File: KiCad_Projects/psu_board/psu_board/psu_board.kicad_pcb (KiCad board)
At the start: 2 copper layers, 21 parts, among them J1 Conn_01x02_Female, J2 Conn_01x02_Female, J3 Conn_01x02_Female, SW1 SW_DIP_x01, SW2 SW_DIP_x01, U1 OKL-T_6-W12N-C

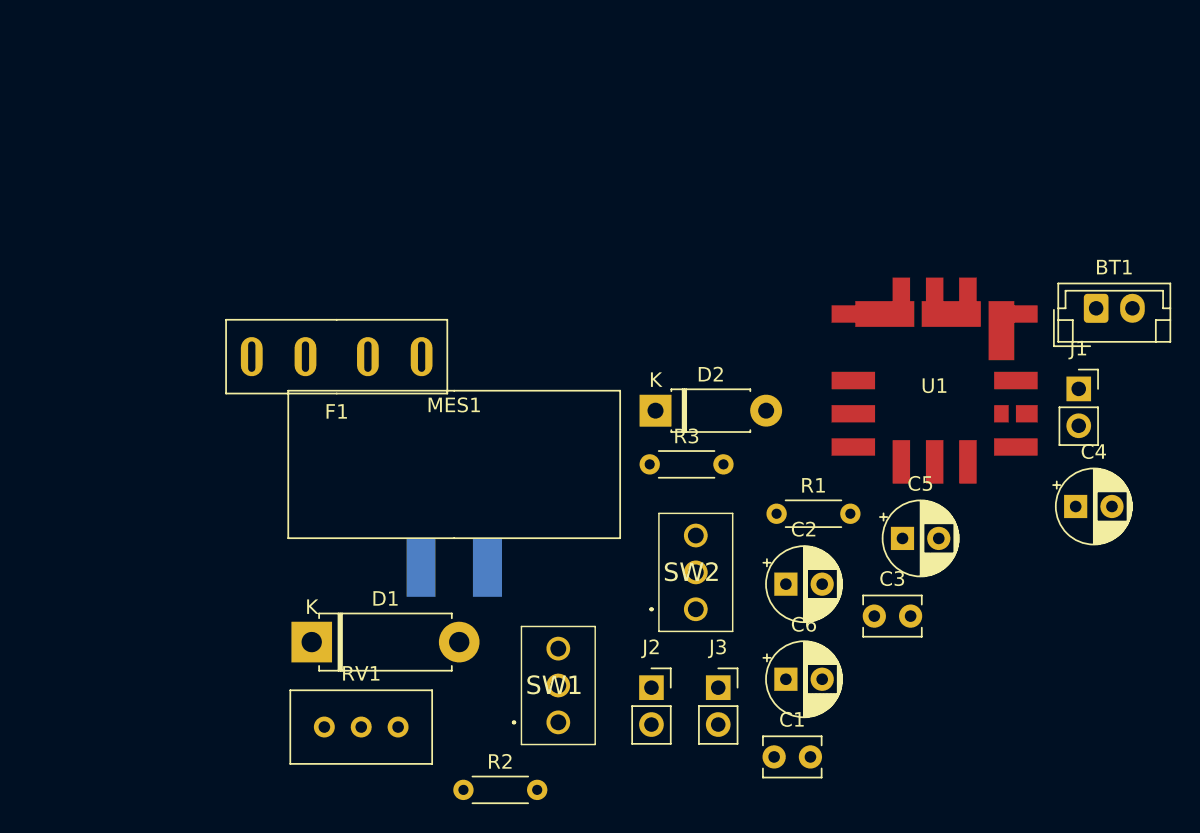
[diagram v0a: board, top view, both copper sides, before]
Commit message: 基盤データの更新
フットプリントの更新、電源基盤の部品の配置
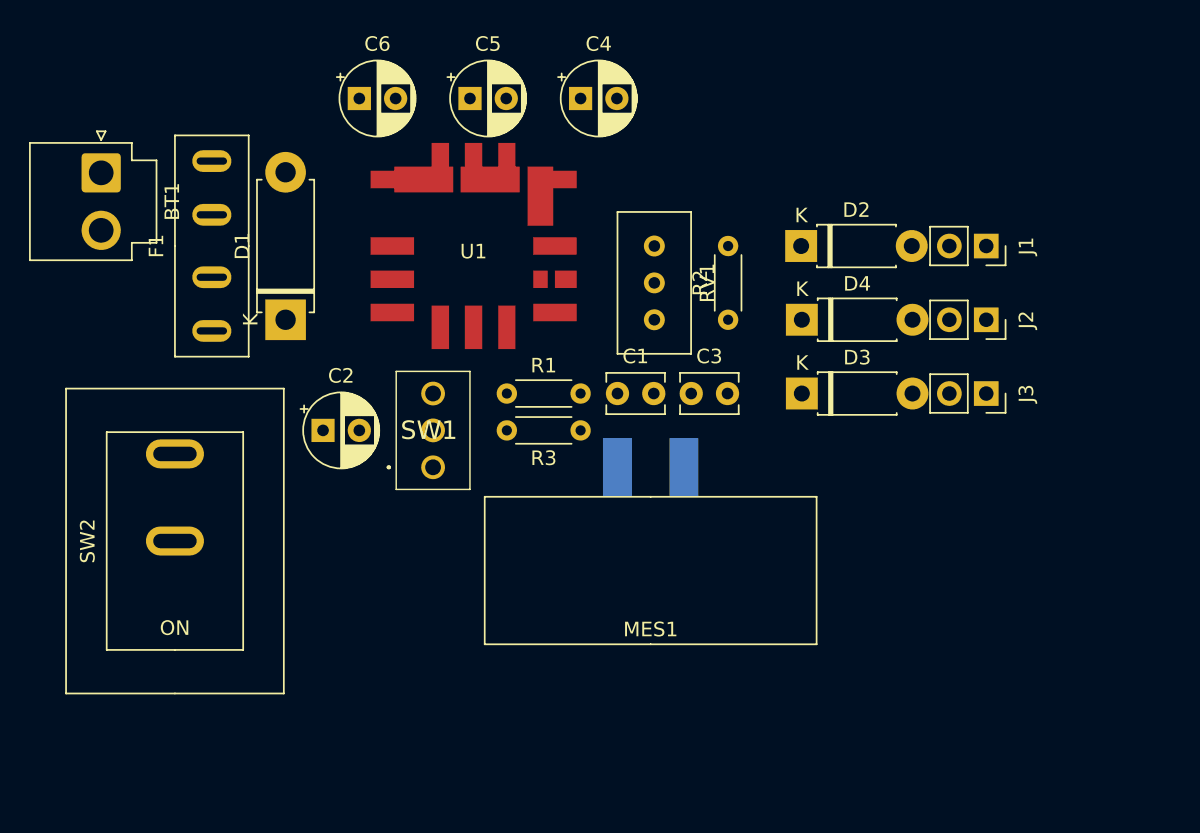
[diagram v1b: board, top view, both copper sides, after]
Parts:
- added D3: D, Diode_THT:D_DO-41_SOD81_P7.62mm_Horizontal, F.Cu at (154.9, 83.8)
- added D4: D, Diode_THT:D_DO-41_SOD81_P7.62mm_Horizontal, F.Cu at (154.9, 78.7)
- BT1: footprint Connector_JST:JST_EH_B2B-EH-A_1x02_P2.50mm_Vertical -> Connector_JST:JST_VH_B2P-VH-B_1x02_P3.96mm_Vertical
- SW2: footprint Lib:2MS1T2B4M2QES -> Lib:DS-850k
- moved BT1 69.2 mm to (106.7, 68.6), turned to -90 degrees
- moved C6 49.6 mm to (124.5, 63.5)
- moved C4 44.2 mm to (139.7, 63.5)
- moved C5 42.5 mm to (132.1, 63.5)
- moved R2 37.2 mm to (149.9, 78.7), turned to 90 degrees
- moved SW2 36.2 mm to (111.8, 94.0), turned to -90 degrees
- moved J2 34.3 mm to (167.6, 78.7), turned to -90 degrees
- moved C2 33.6 mm to (122.0, 86.4)
- moved RV1 33.1 mm to (144.8, 78.7), turned to -90 degrees
- moved U1 33.1 mm to (126.2, 79.8)
- moved J3 27.4 mm to (167.6, 83.8), turned to -90 degrees
- moved C1 27.3 mm to (142.2, 83.8)
- moved D1 22.3 mm to (119.4, 78.7), turned to 90 degrees
- moved MES1 22.1 mm to (144.5, 101.1), turned to 180 degrees
- moved R1 20.3 mm to (134.6, 83.8)
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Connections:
- C3 pad 1: Net-(C3-Pad1) -> +5V
- D2 pad 1: +5V -> Net-(D2-Pad1)
- D2 pad 2: Net-(C3-Pad1) -> +7.5V
- J1 pad 1: +7.5V -> Net-(D2-Pad1)
- J2 pad 1: +7.5V -> Net-(D4-Pad1)
- J3 pad 1: +5V -> Net-(D3-Pad1)
- R3 pad 1: Net-(C3-Pad1) -> +5V
- U1 pad 4: Net-(C3-Pad1) -> +5V
- U1 pad 5: Net-(C3-Pad1) -> +5V

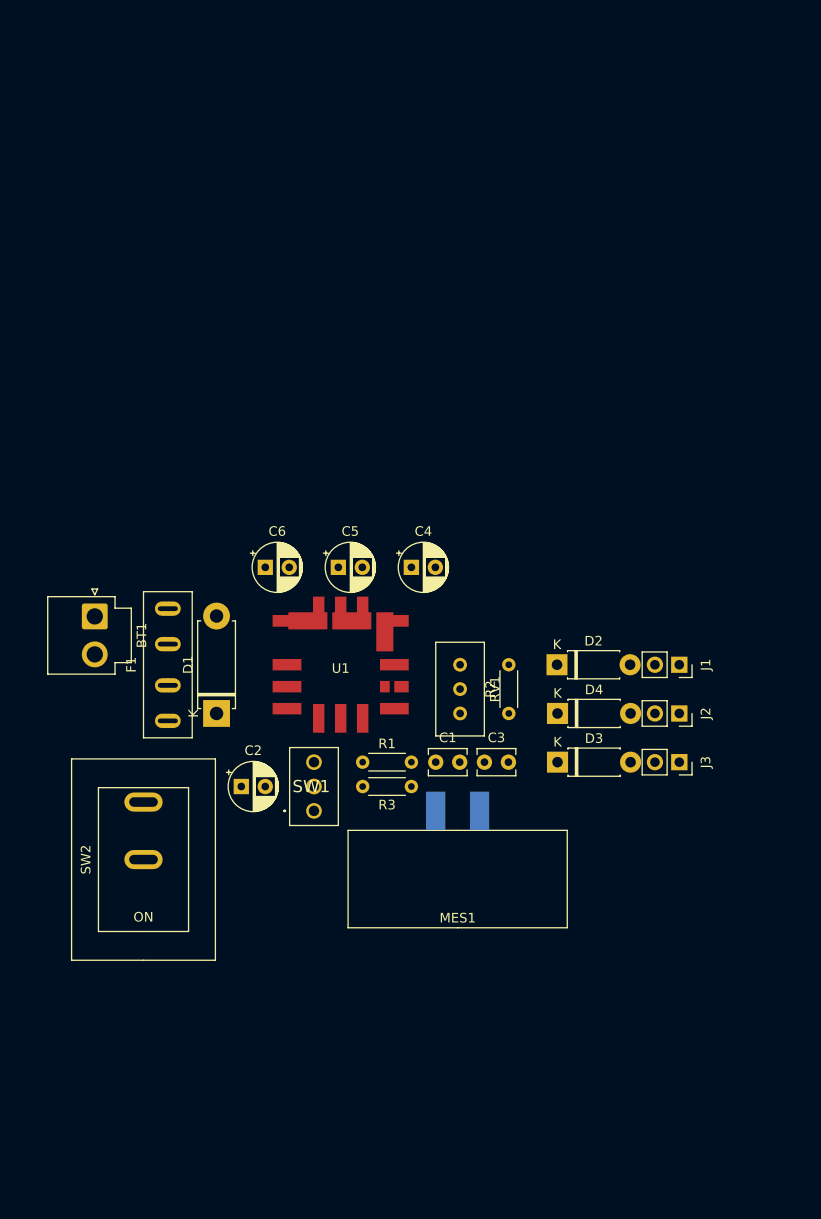
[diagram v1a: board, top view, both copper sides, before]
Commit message: 電源基盤の更新
基盤の外形のインポート、部品の配置。
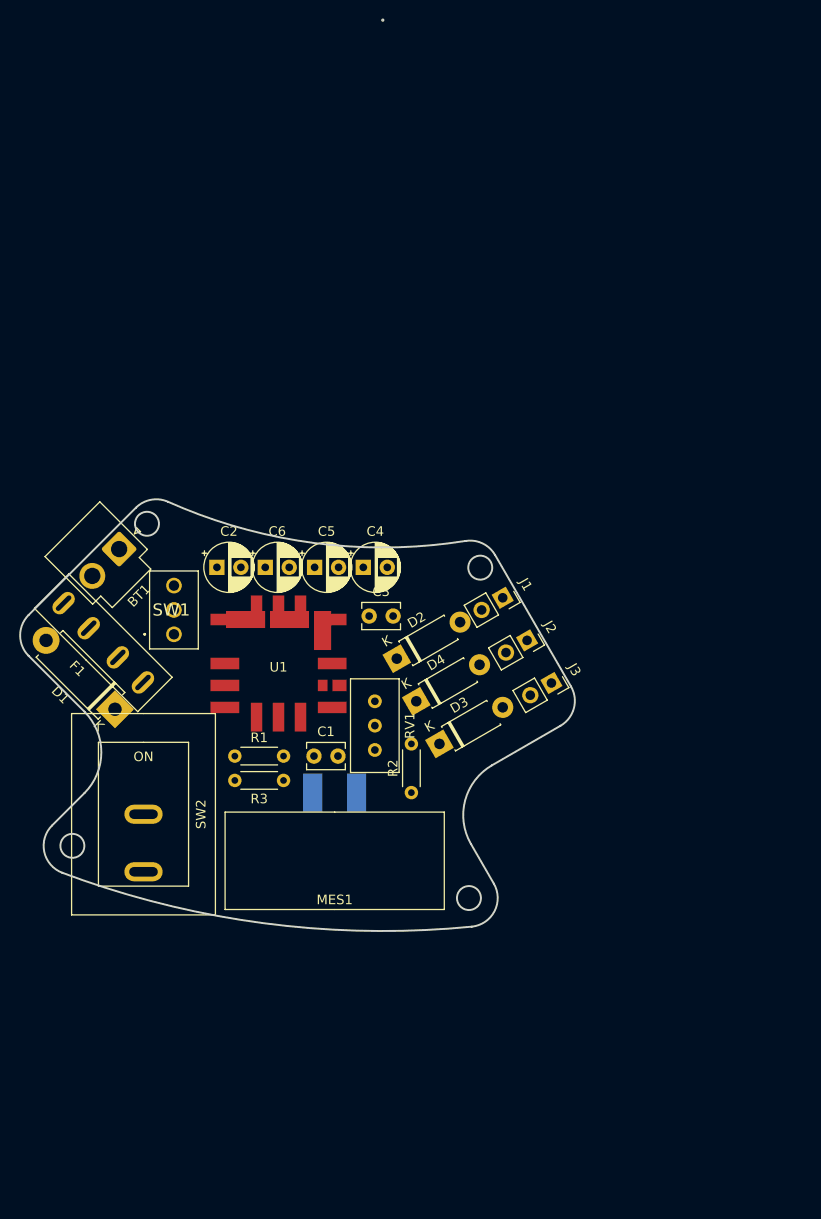
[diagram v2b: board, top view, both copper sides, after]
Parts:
- moved SW1 23.5 mm to (114.9, 70.5)
- moved C2 23.0 mm to (119.4, 63.5)
- moved J1 19.7 mm to (149.2, 66.7), turned to -60 degrees
- moved C3 19.4 mm to (135.3, 68.6)
- moved J2 17.6 mm to (151.8, 71.1), turned to -60 degrees
- moved D2 16.7 mm to (138.2, 73.0), turned to 30 degrees
- moved J3 15.7 mm to (154.3, 75.6), turned to -60 degrees
- moved D4 14.8 mm to (140.2, 77.5), turned to 30 degrees
- moved R1 13.4 mm to (121.3, 83.2)
- moved R3 13.4 mm to (126.4, 85.7)
- moved R2 13.1 mm to (139.7, 87.0)
- moved MES1 13.0 mm to (131.7, 99.2)
- moved C1 12.7 mm to (129.5, 83.2)
- moved D3 12.5 mm to (142.6, 81.9), turned to 30 degrees
- moved D1 10.6 mm to (108.8, 78.3), turned to 135 degrees
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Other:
- board outline added: 57.9 x 95.1 mm

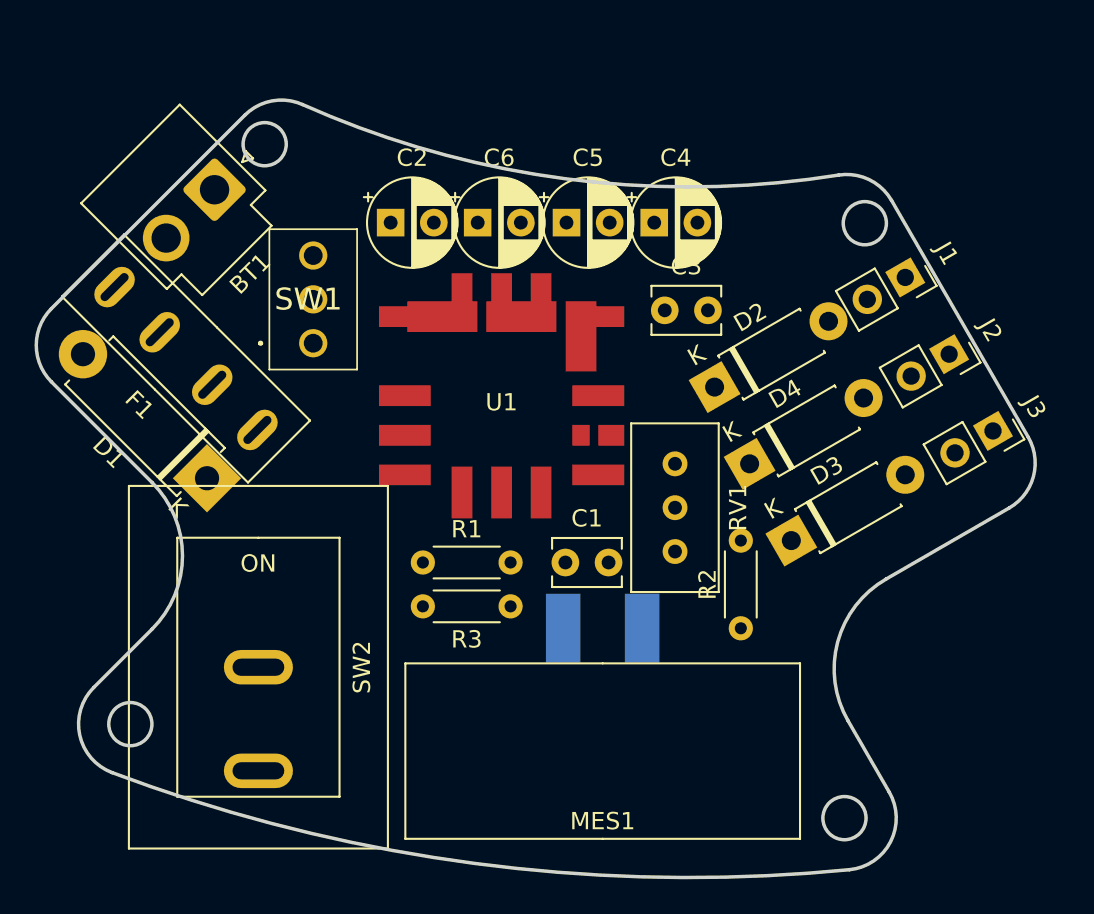
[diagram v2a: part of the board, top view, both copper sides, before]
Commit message: 基盤データの更新
電源基盤、IOボードの配線更新。
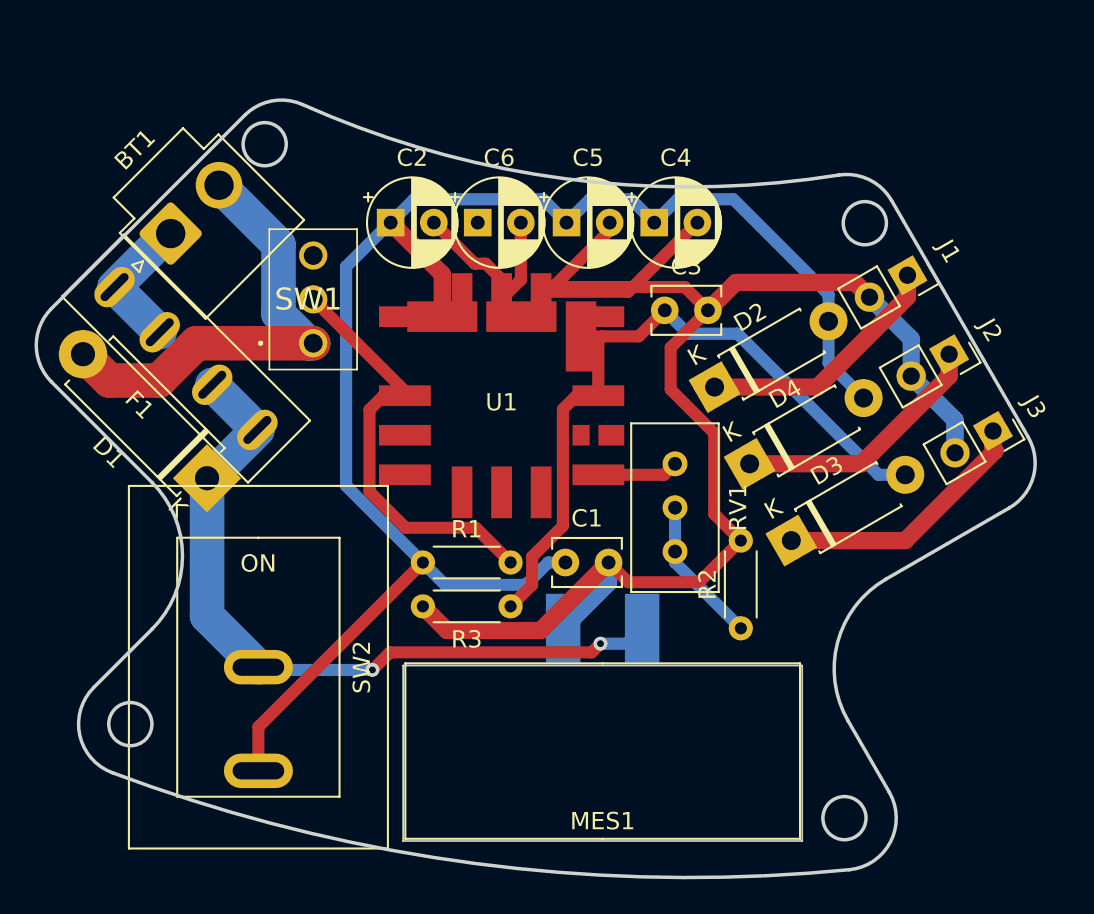
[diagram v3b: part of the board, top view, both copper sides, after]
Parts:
- moved BT1 3.59 mm to (106.7, 64.1), turned to 45 degrees
- moved J1 0.18 mm to (149.4, 66.5)
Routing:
- net GND: track 0.00 -> 131.3 mm
- net +7.5V: track 0.00 -> 91.9 mm
- net Net-(D1-Pad1): track 0.00 -> 43.5 mm, vias 0 -> 2
- net +5V: track 0.00 -> 42.4 mm
- net Net-(R1-Pad2): track 0.00 -> 24.8 mm
- net Net-(D3-Pad1): track 0.00 -> 15.2 mm
- net Net-(D4-Pad1): track 0.00 -> 14.9 mm
- net Net-(D2-Pad1): track 0.00 -> 14.6 mm
- net Net-(R2-Pad1): track 0.00 -> 9.20 mm
- net Net-(BT1-Pad1): track 0.00 -> 8.39 mm
- net Net-(RV1-Pad3): track 0.00 -> 4.71 mm
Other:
- outline, holes or cut-outs redrawn

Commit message: 基盤データのアップデート
ローカルコミットはちゃんと作ってください
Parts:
- removed D2, D3, D4: D, Diode_THT:D_DO-41_SOD81_P7.62mm_Horizontal
- C6: footprint Capacitor_THT:CP_Radial_D5.0mm_P2.50mm -> Capacitor_THT:C_Disc_D3.8mm_W2.6mm_P2.50mm
- moved SW2 54.4 mm to (157.7, 118.4)
- moved C6 46.2 mm to (132.6, 109.0), turned to 180 degrees
- moved C2 46.1 mm to (136.9, 106.2)
- moved C1 46.0 mm to (166.9, 110.0), turned to 30 degrees
- moved C4 41.8 mm to (157.8, 98.3)
- moved C5 40.4 mm to (157.7, 92.5)
- moved SW1 36.3 mm to (135.9, 100.1)
- moved RV1 34.6 mm to (162.3, 104.9), turned to 0 degrees
- moved R1 34.2 mm to (143.8, 109.0)
- moved F1 33.8 mm to (128.8, 97.3)
- moved BT1 33.6 mm to (128.3, 89.9), turned to -45 degrees
- moved D1 33.4 mm to (127.5, 105.9)
- moved J1 33.3 mm to (165.4, 95.8), turned to 120 degrees
- moved J2 33.2 mm to (168.0, 100.1), turned to 120 degrees
- moved J3 33.2 mm to (170.1, 104.7), turned to 120 degrees
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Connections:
- J1 pad 1: Net-(D2-Pad1) -> +7.5V
- J2 pad 1: Net-(D4-Pad1) -> +7.5V
- J3 pad 1: Net-(D3-Pad1) -> +5V
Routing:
- net GND: track 131.3 -> 146.5 mm
- net Net-(D3-Pad1): track 15.2 -> 0.00 mm
- net Net-(D4-Pad1): track 14.9 -> 0.00 mm
- net Net-(D2-Pad1): track 14.6 -> 0.00 mm
- net +5V: track 42.4 -> 51.8 mm
- net +7.5V: track 91.9 -> 100.1 mm, vias 0 -> 1
- net Net-(R2-Pad1): track 9.20 -> 14.2 mm
- net Net-(D1-Pad1): track 43.5 -> 46.9 mm, vias 2 -> 1
- net Net-(BT1-Pad1): track 8.39 -> 11.2 mm
- net Net-(R1-Pad2): track 24.8 -> 23.5 mm, vias 0 -> 1
- net Net-(RV1-Pad3): track 4.71 -> 5.62 mm
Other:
- outline, holes or cut-outs redrawn

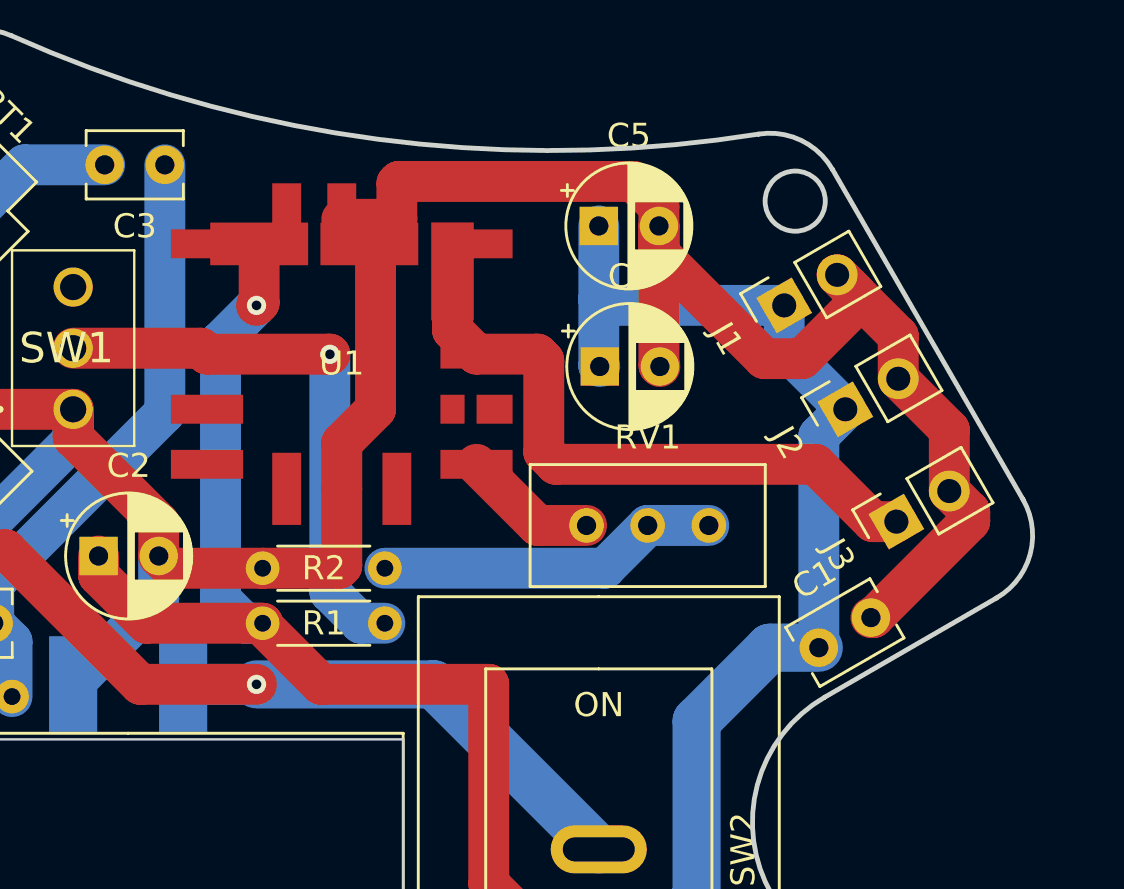
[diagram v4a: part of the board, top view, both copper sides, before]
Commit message: 基板データの更新
IO基板、ライン基板、電源基盤のコネクタ変更、最終確認
メイン基板制作中。
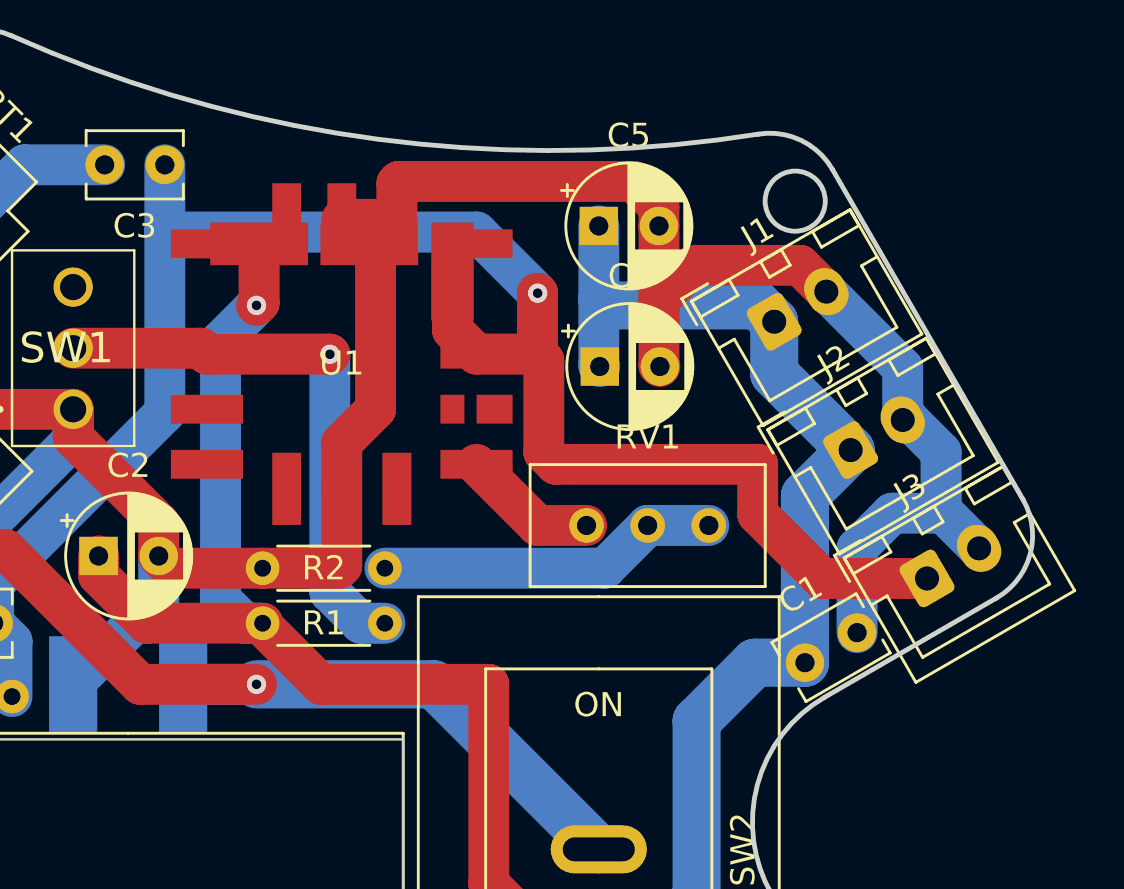
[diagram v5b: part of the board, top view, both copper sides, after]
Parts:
- J1, J2, J3: footprint Connector_PinSocket_2.54mm:PinSocket_1x02_P2.54mm_Vertical -> Connector_JST:JST_XH_B2B-XH-A_1x02_P2.50mm_Vertical
- moved J3 2.68 mm to (171.4, 107.1), turned to 30 degrees
- moved J2 1.71 mm to (168.2, 101.8), turned to 30 degrees
- moved C1 0.85 mm to (166.3, 110.6)
- moved J1 0.80 mm to (165.0, 96.4), turned to 30 degrees
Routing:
- net +5V: track 51.8 -> 74.3 mm, vias 0 -> 1
- net GND: track 146.5 -> 145.8 mm
